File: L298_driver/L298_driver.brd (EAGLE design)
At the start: 100 x 80 mm, 23 parts, among them U1 L298

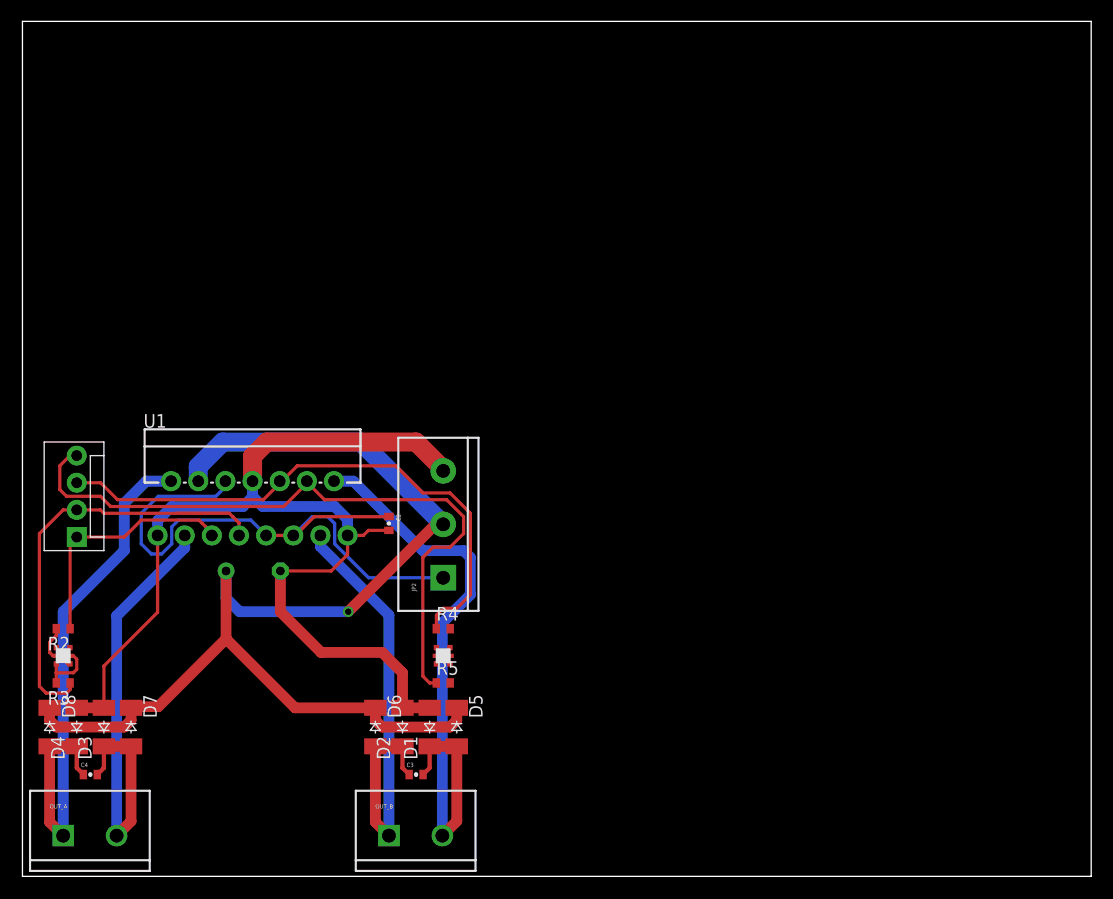
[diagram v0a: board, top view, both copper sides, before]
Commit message: Rearrange components to fit inside triangular board.
Still need to find a place for LEDs and their resistors.
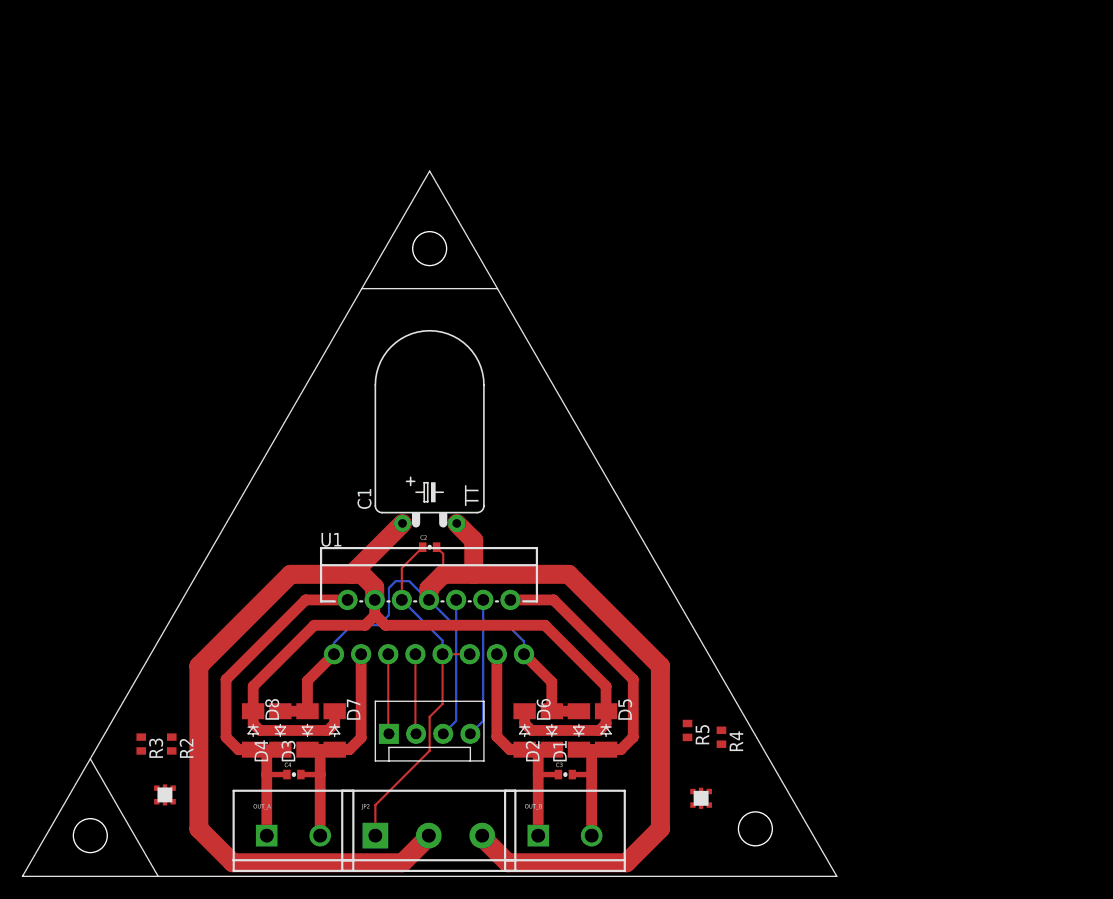
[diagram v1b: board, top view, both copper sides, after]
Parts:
- moved JP1 34.5 mm to (34.3, 13.3), turned to 0 degrees
- moved R4 27.9 mm to (65.4, 13.0), turned to 270 degrees
- moved LED_B 27.6 mm to (63.5, 7.30), turned to 0 degrees
- moved JP2 25.0 mm to (33.0, 3.81), turned to 0 degrees
- moved R5 23.3 mm to (62.2, 13.7), turned to 270 degrees
- moved U1 19.9 mm to (38.1, 23.2)
- moved D3 19.1 mm to (26.7, 13.7)
- moved D7 19.1 mm to (29.2, 13.7)
- moved D8 19.1 mm to (21.6, 13.7)
- moved D4 19.1 mm to (24.1, 13.7)
- moved OUT_A 19.1 mm to (22.9, 3.81)
- moved C4 19.0 mm to (25.4, 9.53)
- moved C1 17.1 mm to (38.1, 33.0), flipped to the top, turned to 0 degrees
- moved LED_A 16.1 mm to (13.3, 7.62), turned to 0 degrees
- moved R2 14.8 mm to (14.0, 12.4), turned to 270 degrees
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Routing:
- net IN4: track 64.1 -> 13.0 mm
- net IN3: track 53.7 -> 13.0 mm
- net IN2: track 39.5 -> 7.48 mm
- net 5V: track 57.7 -> 34.5 mm
- net VCC: track 110.7 -> 133.2 mm, vias 1 -> 0
- net OUT2: track 45.1 -> 23.2 mm
- net OUT4: track 57.2 -> 35.4 mm
- net OUT3: track 45.1 -> 23.4 mm
- net OUT1: track 53.1 -> 35.5 mm
- net IN1: track 22.9 -> 7.48 mm
- net GND: track 102.8 -> 113.5 mm
- net N$2: track 5.45 -> 0.00 mm
- net N$1: track 4.83 -> 0.00 mm
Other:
- board outline removed

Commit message: Finish layout.
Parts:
- moved R5 2.93 mm to (62.9, 10.8)
- moved R4 2.56 mm to (64.1, 10.8)
- moved R3 1.85 mm to (12.1, 10.8)
- moved R2 1.71 mm to (13.3, 10.8)
- moved LED_A 0.90 mm to (12.7, 6.99)
- moved LED_B 0.32 mm to (63.5, 6.99)
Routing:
- net IN2: track 7.48 -> 37.7 mm, vias 0 -> 1
- net IN3: track 13.0 -> 43.1 mm, vias 0 -> 1
- net IN4: track 13.0 -> 37.8 mm, vias 0 -> 1
- net IN1: track 7.48 -> 32.1 mm, vias 0 -> 1
- net GND: track 113.5 -> 121.4 mm
- net N$4: track 0.00 -> 6.67 mm
- net N$2: track 0.00 -> 6.67 mm
- net N$1: track 0.00 -> 4.37 mm
- net N$3: track 0.00 -> 2.69 mm
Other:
- board text added: "SY"

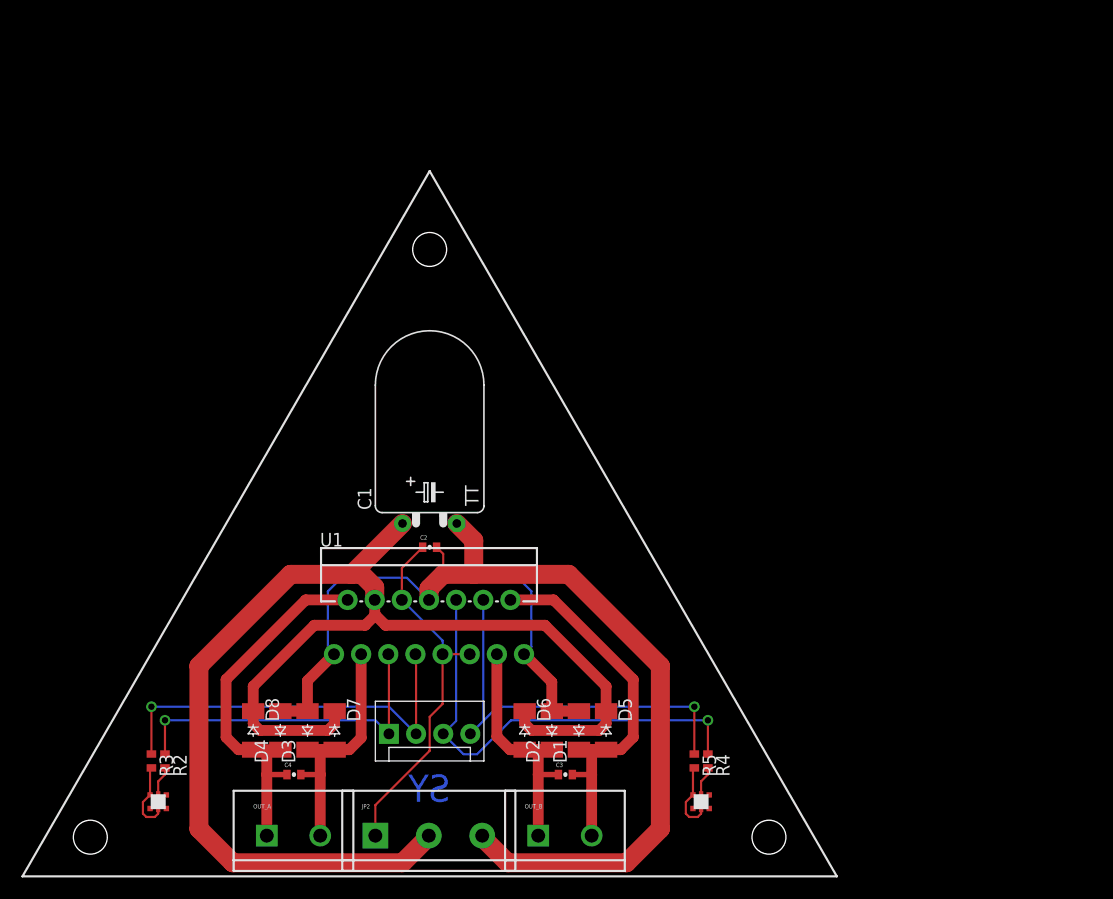
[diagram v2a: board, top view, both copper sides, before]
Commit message: Pour ground planes.
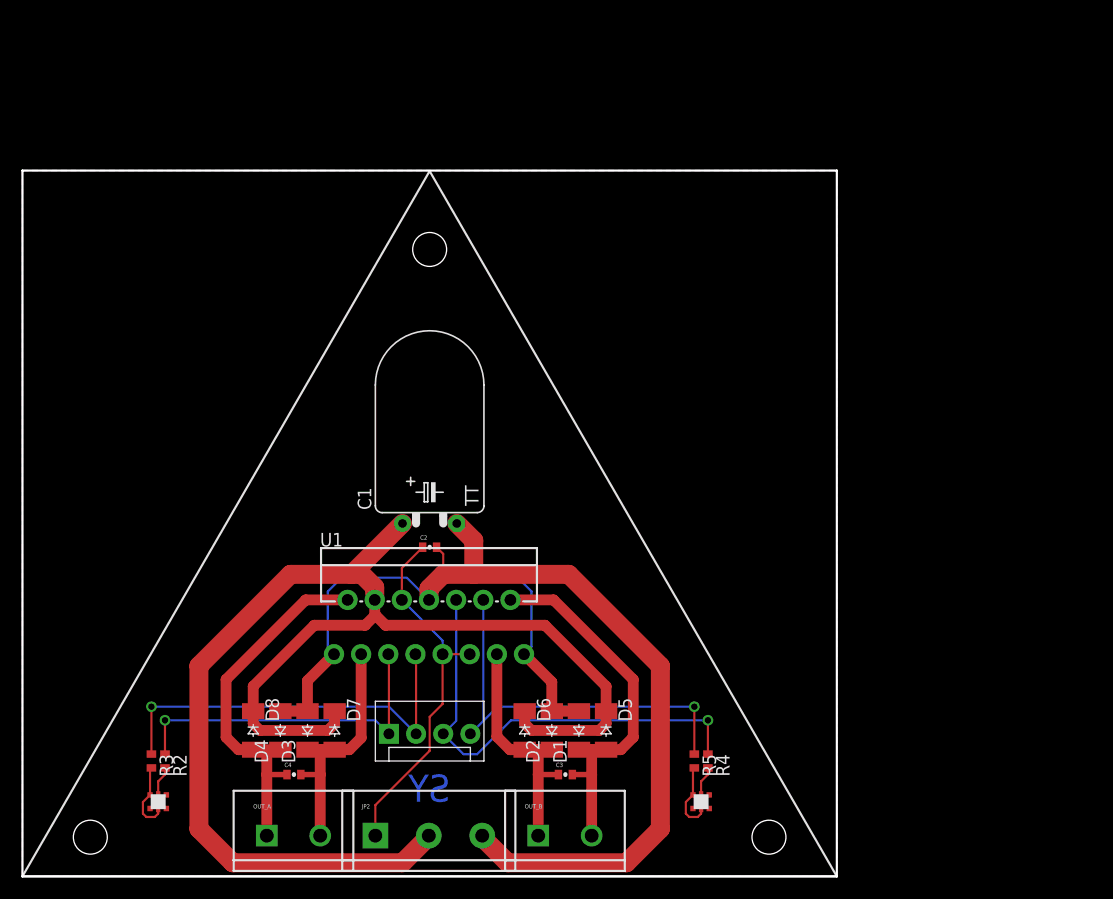
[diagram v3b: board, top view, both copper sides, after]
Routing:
- added copper zone on layer 1, net GND
- added copper zone on layer 16, net GND
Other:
- board outline added: 76.2 x 66 mm
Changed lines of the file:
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@@
 <wire x1="76.2" y1="0" x2="0" y2="0" width="0.2032" layer="121"/>
 <text x="40.005" y="6.985" size="2.54" layer="16" rot="MR0">SY</text>
+<wire x1="0" y1="0" x2="0" y2="66.04" width="0.2032" layer="20"/>
+<wire x1="0" y1="66.04" x2="76.2" y2="66.04" width="0.2032" layer="20"/>
+<wire x1="76.2" y1="66.04" x2="76.2" y2="0" width="0.2032" layer="20"/>
+<wire x1="76.2" y1="0" x2="0" y2="0" width="0.2032" layer="20"/>
 </plain>
 <attributes>
@@
 <wire x1="40.005" y1="27.94" x2="38.04" y2="25.975" width="0.2032" layer="16"/>
 <wire x1="38.04" y1="25.975" x2="38.04" y2="25.8675" width="0.2032" layer="16"/>
+<polygon width="0.2032" layer="1" thermals="no">
+<vertex x="0" y="0"/>
+<vertex x="0" y="66.04"/>
+<vertex x="76.2" y="66.04"/>
+<vertex x="76.2" y="0"/>
+</polygon>
+<polygon width="0.2032" layer="16" thermals="no">
+<vertex x="0" y="0"/>
+<vertex x="0" y="66.04"/>
+<vertex x="76.2" y="66.04"/>
+<vertex x="76.2" y="0"/>
+</polygon>
 </signal>
 <signal name="VCC">

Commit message: Change resistor value for 3.3V operation.
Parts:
- R2, R3, R4, R5: value 249R -> 165R
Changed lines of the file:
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@@
 <element name="D1" library="diode" package="SOD-123_MINI-SMA" value="CGRM4001-G" x="52.07" y="13.6525" rot="R90"/>
 <element name="OUT_A" library="SparkFun-Connectors" package="SCREWTERMINAL-5MM-2" value="" x="22.86" y="3.81"/>
-<element name="R2" library="resistor" package="R0402" value="249R" x="13.335" y="10.795" rot="R270"/>
+<element name="R2" library="resistor" package="R0402" value="165R" x="13.335" y="10.795" rot="R270"/>
 <element name="LED_A" library="yoos" package="6-SMD" value="LRTB_R98G" x="12.7" y="6.985"/>
 <element name="JP2" library="SparkFun-Connectors" package="SCREWTERMINAL-5MM-3" value="" x="33.02" y="3.81"/>
 <element name="LED_B" library="yoos" package="6-SMD" value="LRTB_R98G" x="63.5" y="6.985"/>
-<element name="R3" library="resistor" package="R0402" value="249R" x="12.065" y="10.795" rot="R270"/>
-<element name="R4" library="resistor" package="R0402" value="249R" x="64.135" y="10.795" rot="R270"/>
-<element name="R5" library="resistor" package="R0402" value="249R" x="62.865" y="10.795" rot="R270"/>
+<element name="R3" library="resistor" package="R0402" value="165R" x="12.065" y="10.795" rot="R270"/>
+<element name="R4" library="resistor" package="R0402" value="165R" x="64.135" y="10.795" rot="R270"/>
+<element name="R5" library="resistor" package="R0402" value="165R" x="62.865" y="10.795" rot="R270"/>
 <element name="OUT_B" library="SparkFun-Connectors" package="SCREWTERMINAL-5MM-2" value="" x="48.26" y="3.81"/>
 <element name="D2" library="diode" package="SOD-123_MINI-SMA" value="CGRM4001-G" x="49.53" y="13.6525" rot="R90"/>

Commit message: Finish up.
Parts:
- moved JP1 7.68 mm to (41.9, 14.3), turned to 180 degrees
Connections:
- net IN1: now also JP1.4; no longer JP1.1
- net IN2: now also JP1.3; no longer JP1.2
- net IN3: now also JP1.2; no longer JP1.3
- net IN4: now also JP1.1; no longer JP1.4
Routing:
- net IN4: track 37.8 -> 36.3 mm
- net IN2: track 37.7 -> 36.3 mm, vias 1 -> 2
- net IN1: track 32.1 -> 30.8 mm
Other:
- outline, holes or cut-outs redrawn
- board text added: "1"
- board text added: "2"
- board text added: "3"
- board text added: "4"
- board text added: "5V"
- board text added: "GND"
- board text added: "VS"
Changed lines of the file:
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@@
 <setting verticaltext="up"/>
 </settings>
-<grid distance="0.025" unitdist="inch" unit="inch" style="lines" multiple="1" display="yes" altdistance="0.025" altunitdist="inch" altunit="inch"/>
+<grid distance="0.1" unitdist="inch" unit="inch" style="lines" multiple="1" display="yes" altdistance="0.025" altunitdist="inch" altunit="inch"/>
 <layers>
 <layer number="1" name="Top" color="4" fill="1" visible="yes" active="yes"/>
@@
 <hole x="69.85" y="3.6662375" drill="3.175"/>
 <hole x="38.1" y="58.658759375" drill="3.175"/>
-<wire x1="0" y1="0" x2="38.1" y2="65.991740625" width="0.2032" layer="121"/>
-<wire x1="38.1" y1="65.991740625" x2="76.2" y2="0" width="0.2032" layer="121"/>
-<wire x1="76.2" y1="0" x2="0" y2="0" width="0.2032" layer="121"/>
-<text x="40.005" y="6.985" size="2.54" layer="16" rot="MR0">SY</text>
-<wire x1="0" y1="0" x2="0" y2="66.04" width="0.2032" layer="20"/>
-<wire x1="0" y1="66.04" x2="76.2" y2="66.04" width="0.2032" layer="20"/>
-<wire x1="76.2" y1="66.04" x2="76.2" y2="0" width="0.2032" layer="20"/>
+<wire x1="0" y1="0" x2="38.1" y2="65.991740625" width="0.2032" layer="20"/>
+<wire x1="38.1" y1="65.991740625" x2="76.2" y2="0" width="0.2032" layer="20"/>
 <wire x1="76.2" y1="0" x2="0" y2="0" width="0.2032" layer="20"/>
+<text x="40.3225" y="6.985" size="2.54" layer="16" rot="MR0">SY</text>
+<wire x1="76.2" y1="0" x2="0" y2="0" width="0.2032" layer="20"/>
+<text x="32.0675" y="8.89" size="1.27" layer="20">5V</text>
+<text x="36.83" y="8.89" size="1.27" layer="20">VS</text>
+<text x="40.9575" y="8.89" size="1.27" layer="20">GND</text>
+<text x="33.782" y="17.272" size="1.27" layer="20">1</text>
+<text x="36.322" y="17.272" size="1.27" layer="20">2</text>
+<text x="38.862" y="17.272" size="1.27" layer="20">3</text>
+<text x="41.402" y="17.272" size="1.27" layer="20">4</text>
 </plain>
 <attributes>
@@
 <param name="mtCopper" value="0.035mm 0.035mm 0.035mm 0.035mm 0.035mm 0.035mm 0.035mm 0.035mm 0.035mm 0.035mm 0.035mm 0.035mm 0.035mm 0.035mm 0.035mm 0.035mm"/>
 <param name="mtIsolate" value="1.5mm 0.15mm 0.2mm 0.15mm 0.2mm 0.15mm 0.2mm 0.15mm 0.2mm 0.15mm 0.2mm 0.15mm 0.2mm 0.15mm 0.2mm"/>
-<param name="mdWireWire" value="8mil"/>
-<param name="mdWirePad" value="8mil"/>
-<param name="mdWireVia" value="8mil"/>
+<param name="mdWireWire" value="12mil"/>
+<param name="mdWirePad" value="12mil"/>
+<param name="mdWireVia" value="12mil"/>
 <param name="mdPadPad" value="8mil"/>
 <param name="mdPadVia" value="8mil"/>
@@
 <param name="mdViaViaSameLayer" value="8mil"/>
 <param name="mnLayersViaInSmd" value="2"/>
-<param name="mdCopperDimension" value="40mil"/>
+<param name="mdCopperDimension" value="20mil"/>
 <param name="mdDrill" value="8mil"/>
 <param name="mdSmdStop" value="0mil"/>
@@
 <element name="C3" library="SparkFun-Passives" package="0402-CAP" value="0.1uF" x="50.8" y="9.525"/>
 <element name="C1" library="resistor" package="TT5D11L" value="" x="38.1" y="33.02"/>
-<element name="JP1" library="SparkFun-Connectors" package="MOLEX-1X4" value="" x="34.29" y="13.335"/>
+<element name="JP1" library="SparkFun-Connectors" package="MOLEX-1X4" value="" x="41.91" y="14.2875" rot="R180"/>
 </elements>
 <signals>
@@
 <wire x1="33.9725" y1="23.495" x2="48.895" y2="23.495" width="1.016" layer="1"/>
 <wire x1="35.56" y1="33.02" x2="30.7975" y2="28.2575" width="1.778" layer="1"/>
+<wire x1="38.02" y1="3.81" x2="38.02" y2="3.73" width="1.778" layer="1"/>
 </signal>
 <signal name="5V">
@@
 <signal name="IN1">
 <contactref element="R2" pad="1"/>
-<contactref element="U1" pad="5"/>
-<contactref element="JP1" pad="1"/>
-<wire x1="34.29" y1="13.335" x2="33.02" y2="14.605" width="0.2032" layer="16"/>
-<wire x1="33.02" y1="14.605" x2="13.335" y2="14.605" width="0.2032" layer="16"/>
 <via x="13.335" y="14.605" extent="1-16" drill="0.6"/>
 <wire x1="13.335" y1="14.605" x2="13.335" y2="11.445" width="0.2032" layer="1"/>
+<contactref element="U1" pad="5"/>
+<contactref element="JP1" pad="4"/>
 <wire x1="34.23" y1="20.7875" x2="34.29" y2="20.7275" width="0.2032" layer="1"/>
-<wire x1="34.29" y1="20.7275" x2="34.29" y2="13.335" width="0.2032" layer="1"/>
+<wire x1="34.29" y1="20.7275" x2="34.29" y2="14.2875" width="0.2032" layer="1"/>
+<wire x1="34.29" y1="14.2875" x2="33.9725" y2="14.605" width="0.2032" layer="16"/>
+<wire x1="33.9725" y1="14.605" x2="13.335" y2="14.605" width="0.2032" layer="16"/>
 </signal>
 <signal name="IN2">
 <contactref element="R3" pad="1"/>
-<contactref element="U1" pad="7"/>
-<contactref element="JP1" pad="2"/>
-<wire x1="34.29" y1="15.875" x2="12.065" y2="15.875" width="0.2032" layer="16"/>
 <via x="12.065" y="15.875" extent="1-16" drill="0.6"/>
 <wire x1="12.065" y1="15.875" x2="12.065" y2="11.445" width="0.2032" layer="1"/>
-<wire x1="36.77" y1="20.7875" x2="36.83" y2="20.7275" width="0.2032" layer="1"/>
-<wire x1="36.83" y1="20.7275" x2="36.83" y2="13.335" width="0.2032" layer="1"/>
-<wire x1="34.29" y1="15.875" x2="36.83" y2="13.335" width="0.2032" layer="16"/>
+<contactref element="JP1" pad="3"/>
+<contactref element="U1" pad="7"/>
+<wire x1="36.83" y1="14.2875" x2="36.77" y2="14.3475" width="0.2032" layer="1"/>
+<wire x1="36.77" y1="14.3475" x2="36.77" y2="20.7875" width="0.2032" layer="1"/>
+<via x="36.77" y="14.3475" extent="1-16" drill="0.6"/>
+<wire x1="36.77" y1="14.3475" x2="35.2425" y2="15.875" width="0.2032" layer="16"/>
+<wire x1="35.2425" y1="15.875" x2="12.065" y2="15.875" width="0.2032" layer="16"/>
 </signal>
 <signal name="IN3">
 <contactref element="R4" pad="1"/>
-<contactref element="U1" pad="10"/>
-<contactref element="JP1" pad="3"/>
-<wire x1="40.58" y1="25.8675" x2="40.58" y2="14.545" width="0.2032" layer="16"/>
-<wire x1="40.58" y1="14.545" x2="39.37" y2="13.335" width="0.2032" layer="16"/>
-<wire x1="39.37" y1="13.335" x2="41.275" y2="11.43" width="0.2032" layer="16"/>
-<wire x1="41.275" y1="11.43" x2="42.545" y2="11.43" width="0.2032" layer="16"/>
-<wire x1="42.545" y1="11.43" x2="45.72" y2="14.605" width="0.2032" layer="16"/>
-<wire x1="45.72" y1="14.605" x2="64.135" y2="14.605" width="0.2032" layer="16"/>
 <via x="64.135" y="14.605" extent="1-16" drill="0.6"/>
 <wire x1="64.135" y1="14.605" x2="64.135" y2="11.445" width="0.2032" layer="1"/>
+<contactref element="U1" pad="10"/>
+<contactref element="JP1" pad="2"/>
+<wire x1="40.58" y1="15.4975" x2="40.58" y2="25.8675" width="0.2032" layer="16"/>
+<wire x1="40.58" y1="15.4975" x2="39.37" y2="14.2875" width="0.2032" layer="16"/>
+<wire x1="39.37" y1="14.2875" x2="39.37" y2="12.7" width="0.2032" layer="16"/>
+<wire x1="64.135" y1="14.605" x2="46.355" y2="14.605" width="0.2032" layer="16"/>
+<wire x1="46.355" y1="14.605" x2="43.4975" y2="11.7475" width="0.2032" layer="16"/>
+<wire x1="43.4975" y1="11.7475" x2="42.2275" y2="11.7475" width="0.2032" layer="16"/>
+<wire x1="42.2275" y1="11.7475" x2="40.9575" y2="11.7475" width="0.2032" layer="16"/>
+<wire x1="39.37" y1="12.7" x2="40.3225" y2="11.7475" width="0.2032" layer="16"/>
+<wire x1="40.3225" y1="11.7475" x2="40.9575" y2="11.7475" width="0.2032" layer="16"/>
 </signal>
 <signal name="IN4">
 <contactref element="R5" pad="1"/>
-<contactref element="U1" pad="12"/>
-<contactref element="JP1" pad="4"/>
-<wire x1="43.12" y1="25.8675" x2="43.12" y2="14.545" width="0.2032" layer="16"/>
-<wire x1="43.12" y1="14.545" x2="41.91" y2="13.335" width="0.2032" layer="16"/>
-<wire x1="43.12" y1="14.545" x2="44.45" y2="15.875" width="0.2032" layer="16"/>
-<wire x1="44.45" y1="15.875" x2="62.865" y2="15.875" width="0.2032" layer="16"/>
 <via x="62.865" y="15.875" extent="1-16" drill="0.6"/>
 <wire x1="62.865" y1="15.875" x2="62.865" y2="11.445" width="0.2032" layer="1"/>
+<contactref element="JP1" pad="1"/>
+<contactref element="U1" pad="12"/>
+<wire x1="41.91" y1="14.2875" x2="43.12" y2="15.4975" width="0.2032" layer="16"/>
+<wire x1="43.12" y1="15.4975" x2="43.12" y2="15.875" width="0.2032" layer="16"/>
+<wire x1="43.12" y1="15.875" x2="43.12" y2="25.8675" width="0.2032" layer="16"/>
+<wire x1="62.865" y1="15.875" x2="43.12" y2="15.875" width="0.2032" layer="16"/>
 </signal>
 <signal name="OUT1">
